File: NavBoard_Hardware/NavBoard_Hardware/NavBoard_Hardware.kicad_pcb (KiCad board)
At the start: 2 copper layers, 124.5 x 79.2 mm, 61 parts, among them U1 OKI-5V, U2 ICM-20948, U3 BNO055, U4 OKI-3V3, U5 NEO-M8P-2, U6 Raspberry_Pi

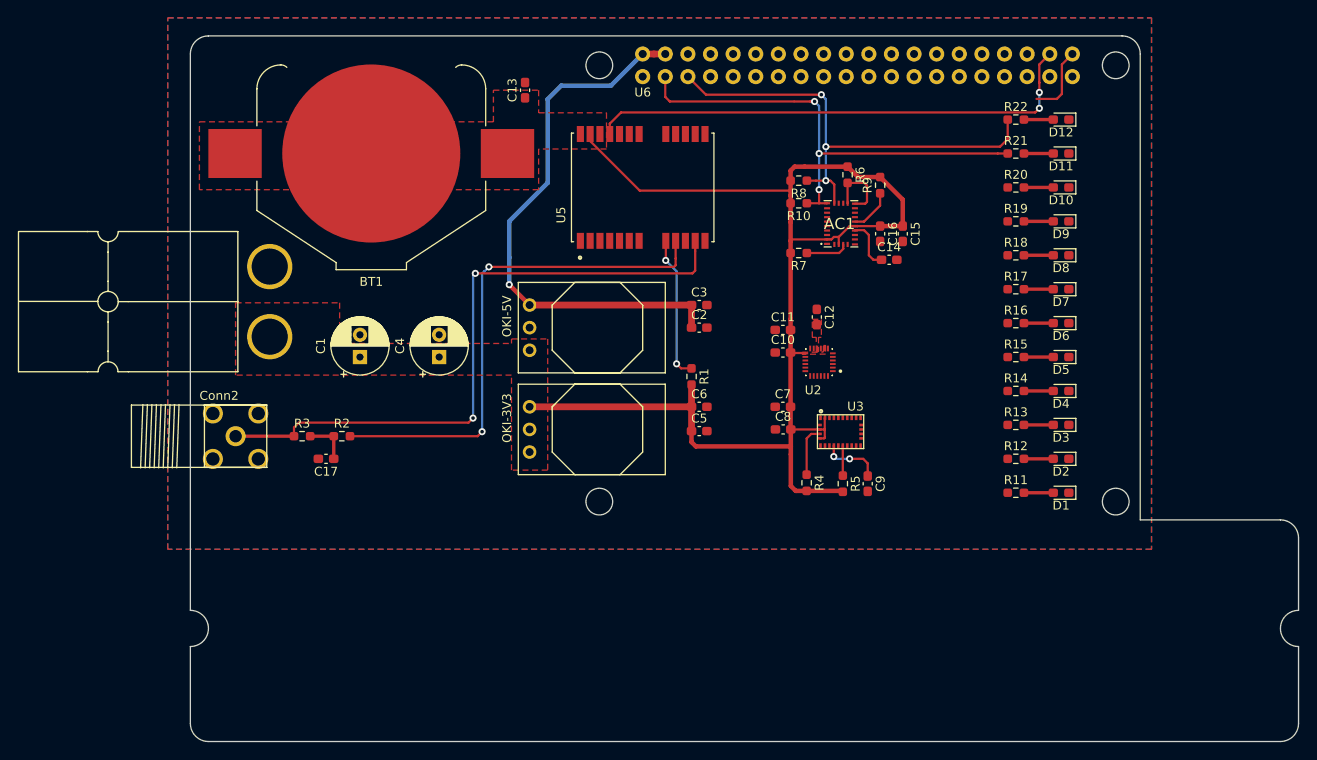
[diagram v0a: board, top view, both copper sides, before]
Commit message: Finished layout for board reviews
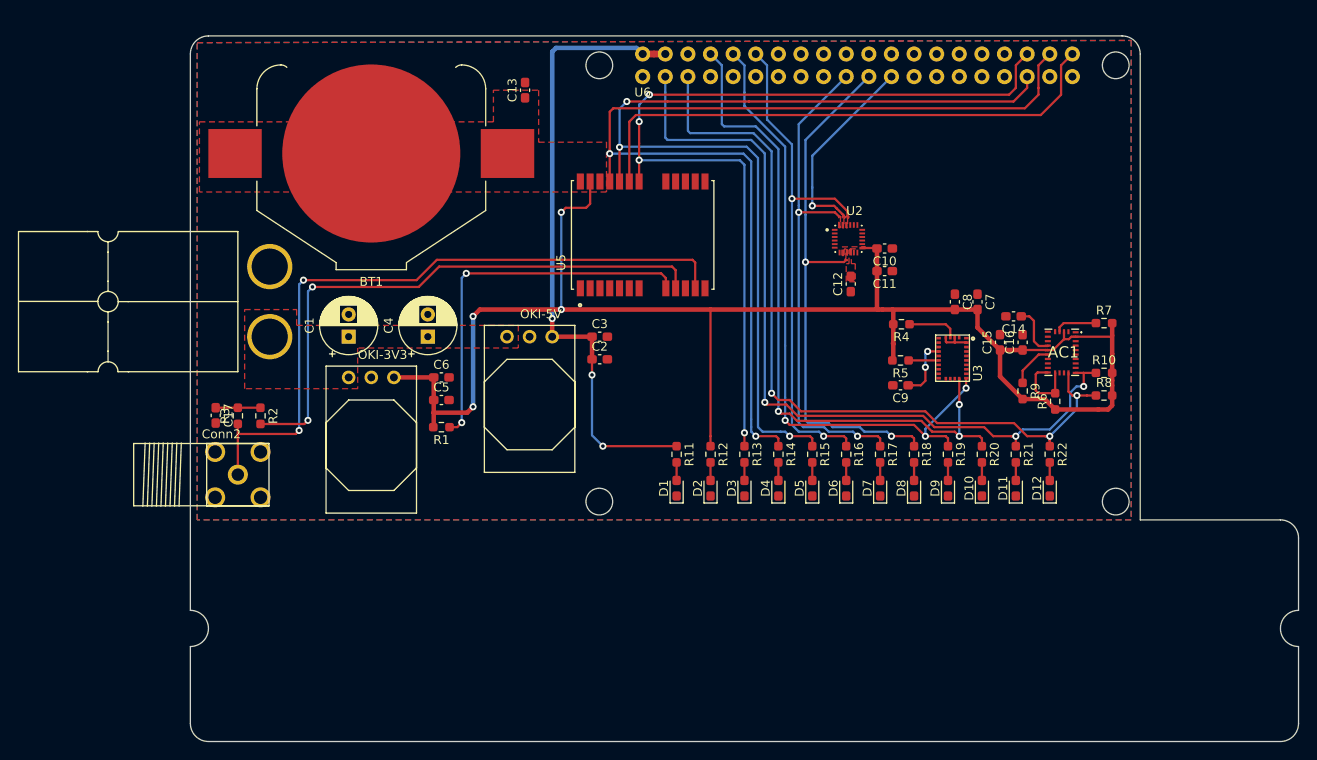
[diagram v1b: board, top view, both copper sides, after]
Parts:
- moved D1 43.2 mm to (80.0, 75.7), turned to 90 degrees
- moved R8 41.9 mm to (128.0, 65.3), turned to 0 degrees
- moved D12 41.4 mm to (121.9, 75.7), turned to 90 degrees
- moved D2 39.5 mm to (83.8, 75.7), turned to 90 degrees
- moved R10 39.2 mm to (128.0, 62.7), turned to 0 degrees
- moved R11 38.3 mm to (80.0, 71.9), turned to 270 degrees
- moved D11 37.9 mm to (118.1, 75.7), turned to 90 degrees
- moved R22 37.8 mm to (121.9, 71.9), turned to 270 degrees
- moved D3 36.3 mm to (87.6, 75.7), turned to 90 degrees
- moved R7 35.2 mm to (128.0, 57.1), turned to 0 degrees
- moved D10 34.9 mm to (114.3, 75.7), turned to 90 degrees
- moved R6 34.5 mm to (122.5, 65.9), turned to 90 degrees
- moved R12 34.3 mm to (83.8, 71.9), turned to 270 degrees
- moved R21 33.8 mm to (118.1, 71.9), turned to 270 degrees
- moved D4 33.6 mm to (91.4, 75.7), turned to 90 degrees
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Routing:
- net M8P_MISO: track 0.00 -> 110.0 mm, vias 0 -> 3
- net M8P_CS: track 0.00 -> 99.7 mm, vias 0 -> 4
- net BNO055_RX: track 0.00 -> 76.8 mm, vias 0 -> 3
- net BNO055_TX: track 0.00 -> 72.0 mm, vias 0 -> 3
- net ICM_MISO: track 0.00 -> 60.1 mm, vias 0 -> 2
- net ICM_CS: track 0.00 -> 58.4 mm, vias 0 -> 2
- net ICM_MOSI: track 0.00 -> 56.6 mm, vias 0 -> 2
- net M8P_MOSI: track 56.7 -> 112.7 mm
- net M8P_CLK: track 8.05 -> 61.6 mm
- net BNO080_SDA: track 54.4 -> 92.7 mm
- net BNO080_SCL: track 54.0 -> 89.7 mm
- net +3V3: track 143.3 -> 178.8 mm, vias 0 -> 4
- net Net-(R1-Pad1): track 16.2 -> 42.3 mm
- net ICM_SCLK: track 0.00 -> 22.3 mm, vias 0 -> 1
- net +5V: track 62.0 -> 70.9 mm, vias 1 -> 3
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- added copper zone on F.Cu, net ICM_CS
- added copper zone on F.Cu, net ICM_MISO
- added copper zone on F.Cu, net ICM_MOSI
- added copper zone on F.Cu, net ICM_SCLK

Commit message: Board Review Edits
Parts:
- moved R7 1.27 mm to (128.0, 55.9)
- moved C12 0.05 mm to (99.5, 52.8)
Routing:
- net GND: track 0.00 -> 129.7 mm, vias 0 -> 17
- net +3V3: track 178.8 -> 190.2 mm, vias 4 -> 6
- net Net-(C12-Pad2): track 0.00 -> 2.69 mm
- net ICM_MISO: track 60.1 -> 61.5 mm
- net Net-(AC1-Pad4): track 4.80 -> 6.03 mm
- net ICM_MOSI: track 56.6 -> 57.5 mm
- net ICM_SCLK: track 22.3 -> 23.2 mm
- net ICM_CS: track 58.4 -> 59.3 mm
- removed copper zone on F.Cu, net +3V3
- removed copper zone on F.Cu, net ICM_CS
- removed copper zone on F.Cu, net ICM_MISO
- removed copper zone on F.Cu, net ICM_MOSI
- removed copper zone on F.Cu, net ICM_SCLK
- removed copper zone on F.Cu, net Net-(C12-Pad2)
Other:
- net class Default: clearance 0.2 -> 0.127; trace_width 0.25 -> 0.254
- rule trace_clearance: 0.2 -> 0.127

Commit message: Deleted old components
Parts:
- removed AC1: BNO080, BNO080:BNO080
- removed BT1: Battery_Cell, Battery:BatteryHolder_Keystone_3008_1x2450
- removed C1, C4: 22uF 50V, Capacitor_THT:CP_Radial_D6.3mm_P2.50mm
- removed C10, C11, C12, C14, C15, C16, C3, C6, C9: 0.1uF, Capacitor_SMD:C_0603_1608Metric_Pad1.08x0.95mm_HandSolder
- removed C13: 1uF, Capacitor_SMD:C_0603_1608Metric_Pad1.08x0.95mm_HandSolder
- removed C17: 47pF, Capacitor_SMD:C_0603_1608Metric_Pad1.08x0.95mm_HandSolder
- removed C2, C5: 10uF, Capacitor_SMD:C_0603_1608Metric_Pad1.08x0.95mm_HandSolder
- removed C7: 6.8nF, Capacitor_SMD:C_0603_1608Metric_Pad1.08x0.95mm_HandSolder
- removed C8: 120nF, Capacitor_SMD:C_0603_1608Metric_Pad1.08x0.95mm_HandSolder
- removed Conn2: RP-SMA, MRDT_Connectors:RP-SMA_Jack_Tru-Hole_Right-Angle
- removed D1, D2: GREEN, LED_SMD:LED_0603_1608Metric_Pad1.05x0.95mm_HandSolder
- removed D10, D11, D12, D3, D4, D5, D6, D7, D8, D9: BLUE, LED_SMD:LED_0603_1608Metric_Pad1.05x0.95mm_HandSolder
- removed R1: 10K, Resistor_SMD:R_0603_1608Metric_Pad0.98x0.95mm_HandSolder
- removed R10, R6, R8: 2.2k, Resistor_SMD:R_0603_1608Metric_Pad0.98x0.95mm_HandSolder
- removed R11, R13, R14, R15, R16, R17, R18, R19, R20, R21, R22: 100, Resistor_SMD:R_0603_1608Metric_Pad0.98x0.95mm_HandSolder
- removed R12: 43, Resistor_SMD:R_0603_1608Metric_Pad0.98x0.95mm_HandSolder
- removed R2: 10, Resistor_SMD:R_0603_1608Metric_Pad0.98x0.95mm_HandSolder
- removed R3: 30@100MHZ/2.0A, Resistor_SMD:R_0603_1608Metric_Pad0.98x0.95mm_HandSolder
- removed R4, R5, R7, R9: 10k, Resistor_SMD:R_0603_1608Metric_Pad0.98x0.95mm_HandSolder
- removed U1: OKI-5V, MRDT_Devices:OKI_Horizontal
- removed U2: ICM-20948, MRDT_ICs:ICM_20948
- removed U3: BNO055, MRDT_ICs:BNO055
- removed U4: OKI-3V3, MRDT_Devices:OKI_Horizontal
- removed U5: NEO-M8P-2, MRDT_ICs:MODULE_NEO-M8P-2
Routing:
- net +3V3: track 190.2 -> 0.00 mm, vias 6 -> 0
- net GND: track 129.7 -> 0.00 mm, vias 17 -> 0
- net M8P_MOSI: track 112.7 -> 0.00 mm, vias 2 -> 0
- net M8P_MISO: track 110.0 -> 0.00 mm, vias 3 -> 0
- net M8P_CS: track 99.7 -> 0.00 mm, vias 4 -> 0
- net BNO080_SDA: track 92.7 -> 0.00 mm, vias 3 -> 0
- net BNO080_SCL: track 89.7 -> 0.00 mm, vias 3 -> 0
- net Net-(Conn2-Pad1): track 77.8 -> 0.00 mm, vias 2 -> 0
- net BNO055_RX: track 76.8 -> 0.00 mm, vias 3 -> 0
- net BNO055_TX: track 72.0 -> 0.00 mm, vias 3 -> 0
- net +5V: track 70.9 -> 0.00 mm, vias 3 -> 0
- net Net-(R2-Pad2): track 64.6 -> 0.00 mm, vias 2 -> 0
- net M8P_CLK: track 61.6 -> 0.00 mm
- net ICM_MISO: track 61.5 -> 0.00 mm, vias 2 -> 0
- net ICM_CS: track 59.3 -> 0.00 mm, vias 2 -> 0
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- removed copper zone on F.Cu, net +12V
- removed copper zone on B.Cu, net GND
- removed copper zone on F.Cu, net GND
- removed copper zone on F.Cu, net V_BCKP
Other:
- board outline removed
